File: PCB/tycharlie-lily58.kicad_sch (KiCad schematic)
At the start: 78 parts, among them J1 Conn_01x02_Pin, J2 Conn_01x05_Pin, J3 AudioJack4, SW1 SW_Push, SW10 SW_Push, SW11 SW_Push, SW12 SW_Push, SW13 SW_Push, SW14 SW_Push, SW15 SW_Push, SW16 SW_Push, SW17 SW_Push, SW18 SW_Push, SW19 SW_Push, SW2 SW_Push, SW20 SW_Push, SW21 SW_Push, SW22 SW_Push, SW23 SW_Push, SW24 SW_Push, SW25 SW_Push, SW26 SW_Push, SW27 SW_Push, SW28 SW_Push, SW29 SW_Push, SW3 SW_Push, SW30 SW_Push, SW4 SW_Push, SW5 SW_Push, SW6 SW_Push, SW7 SW_Push, SW8 SW_Push, SW9 SW_Push, U1 SuperMini nRF52840

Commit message: FEAT: add the dxf file for edge cut - use the dxf file to maintain the edge cut - add two different mounting hole - use larger mounting hole for robustness
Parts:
- H1, H2, H4: footprint tycharlie-lily58:MountingHole_2.2mm_M2_ISO14580_Pad_TopBottom -> tycharlie-lily58:MountingHole_3mm_Oval_Hole_ISO14580_Pad_TopBottom
- H5: footprint tycharlie-lily58:MountingHole_2.2mm_M2_ISO14580_Pad_TopBottom -> tycharlie-lily58:MountingHole_3mm_M2_ISO14580_Pad_TopBottom

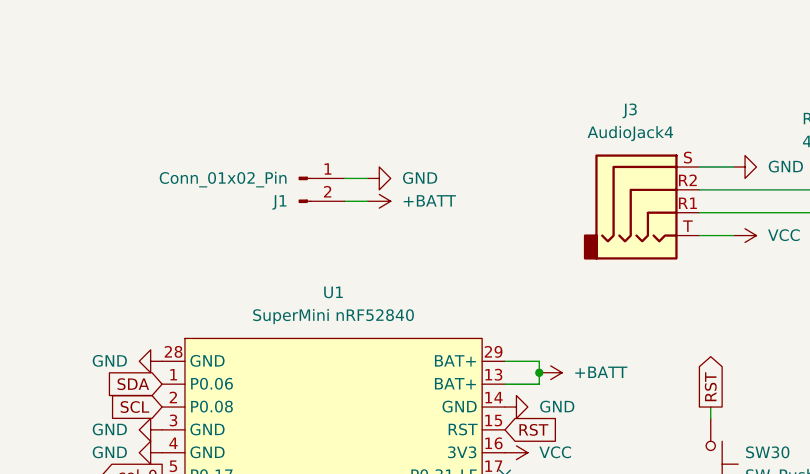
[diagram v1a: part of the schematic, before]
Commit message: FIX: update the battery footprint
  - Add new Molex PicoBlade 53261 foorprint
  - Changed the battery pin1 to BATT+
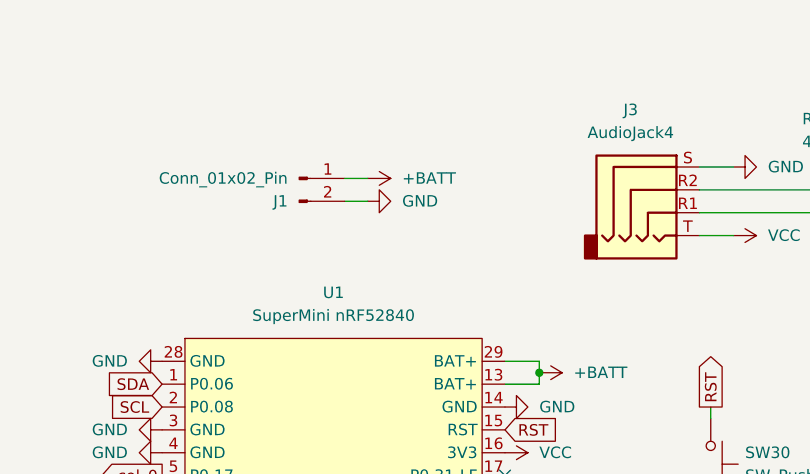
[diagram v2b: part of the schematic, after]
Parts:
- J1: footprint tycharlie-lily58:JST_GH_SM02B-GHS-TB_1x02-1MP_P1.25mm_Horizontal -> tycharlie-lily58:Molex_PicoBlade_53261-0271_1x02-1MP_P1.25mm_Horizontal
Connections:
- net +BATT: now also J1.1 (Pin_1); no longer J1.2 (Pin_2)
- net GND: now also J1.2 (Pin_2); no longer J1.1 (Pin_1)
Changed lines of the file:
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@@
 	(wire
 		(pts
+			(xy 77.47 35.56) (xy 80.01 35.56)
+		)
+		(stroke
+			(width 0)
+			(type default)
+		)
+	)
+	(wire
+		(pts
 			(xy 93.98 101.6) (xy 93.98 128.27)
 		)
@@
 	(wire
 		(pts
+			(xy 77.47 33.02) (xy 80.01 33.02)
+		)
+		(stroke
+			(width 0)
+			(type default)
+		)
+	)
+	(wire
+		(pts
 			(xy 193.04 62.23) (xy 193.04 81.28)
 		)
@@
 	(wire
 		(pts
-			(xy 80.01 33.02) (xy 77.47 33.02)
-		)
-		(stroke
-			(width 0)
-			(type default)
-		)
-	)
-	(wire
-		(pts
 			(xy 99.06 111.76) (xy 99.06 106.68)
 		)
@@
 	(wire
 		(pts
-			(xy 80.01 35.56) (xy 77.47 35.56)
-		)
-		(stroke
-			(width 0)
-			(type default)
-		)
-	)
-	(wire
-		(pts
 			(xy 78.74 135.89) (xy 78.74 149.86)
 		)
@@
 			)
 		)
-		(property "Footprint" "tycharlie-lily58:JST_GH_SM02B-GHS-TB_1x02-1MP_P1.25mm_Horizontal"
+		(property "Footprint" "tycharlie-lily58:Molex_PicoBlade_53261-0271_1x02-1MP_P1.25mm_Horizontal"
 			(at 72.39 33.02 0)
 			(hide yes)
@@
 	(symbol
 		(lib_id "power:GND")
-		(at 80.01 33.02 90)
+		(at 80.01 35.56 90)
 		(unit 1)
 		(body_style 1)
@@
 		(fields_autoplaced yes)
 		(property "Reference" "#PWR01"
-			(at 86.36 33.02 0)
+			(at 86.36 35.56 0)
 			(hide yes)
 			(show_name no)
@@
 		)
 		(property "Value" "GND"
-			(at 83.82 33.0201 90)
+			(at 83.82 35.5601 90)
 			(show_name no)
 			(do_not_autoplace no)
@@
 		)
 		(property "Footprint" ""
-			(at 80.01 33.02 0)
+			(at 80.01 35.56 0)
 			(hide yes)
 			(show_name no)
@@
 		)
 		(property "Datasheet" ""
-			(at 80.01 33.02 0)
+			(at 80.01 35.56 0)
 			(hide yes)
 			(show_name no)
@@
 		)
 		(property "Description" "Power symbol creates a global label with name \"GND\" , ground"
-			(at 80.01 33.02 0)
+			(at 80.01 35.56 0)
 			(hide yes)
 			(show_name no)
@@
 	(symbol
 		(lib_id "power:+BATT")
-		(at 80.01 35.56 270)
+		(at 80.01 33.02 270)
 		(unit 1)
 		(body_style 1)
@@
 		(fields_autoplaced yes)
 		(property "Reference" "#PWR02"
-			(at 76.2 35.56 0)
+			(at 76.2 33.02 0)
 			(hide yes)
 			(show_name no)
@@
 		)
 		(property "Value" "+BATT"
-			(at 83.82 35.5601 90)
+			(at 83.82 33.0201 90)
 			(show_name no)
 			(do_not_autoplace no)
@@
 		)
 		(property "Footprint" ""
-			(at 80.01 35.56 0)
+			(at 80.01 33.02 0)
 			(hide yes)
 			(show_name no)
@@
 		)
 		(property "Datasheet" ""
-			(at 80.01 35.56 0)
+			(at 80.01 33.02 0)
 			(hide yes)
 			(show_name no)
@@
 		)
 		(property "Description" "Power symbol creates a global label with name \"+BATT\""
-			(at 80.01 35.56 0)
+			(at 80.01 33.02 0)
 			(hide yes)
 			(show_name no)
